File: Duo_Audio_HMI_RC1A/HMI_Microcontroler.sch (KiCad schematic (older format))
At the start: 28 parts, among them P4 HEADER_5X2_P0.05, U1 LPC175XFBD80, U2 TLV803, U3 74LVC1G125, X1 10MHz

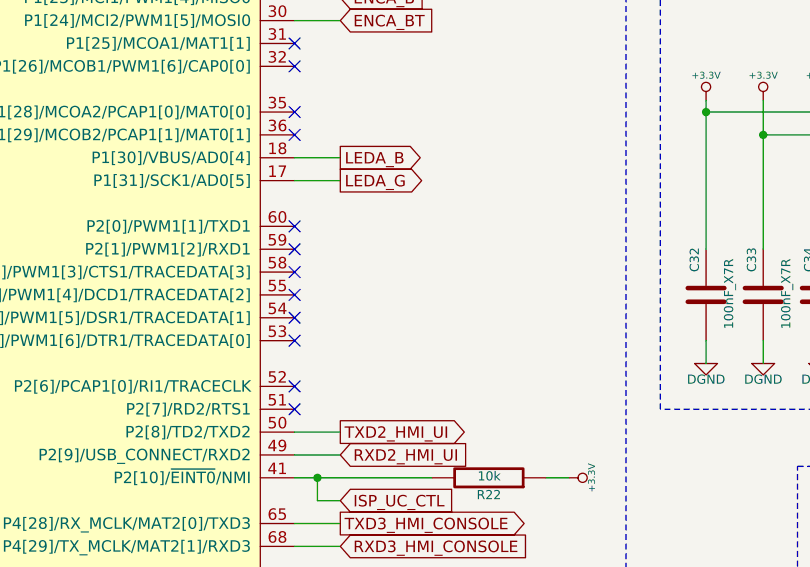
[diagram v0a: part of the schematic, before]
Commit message: Implementing RCA1 schematic  modifications for new layout. Backup commit.
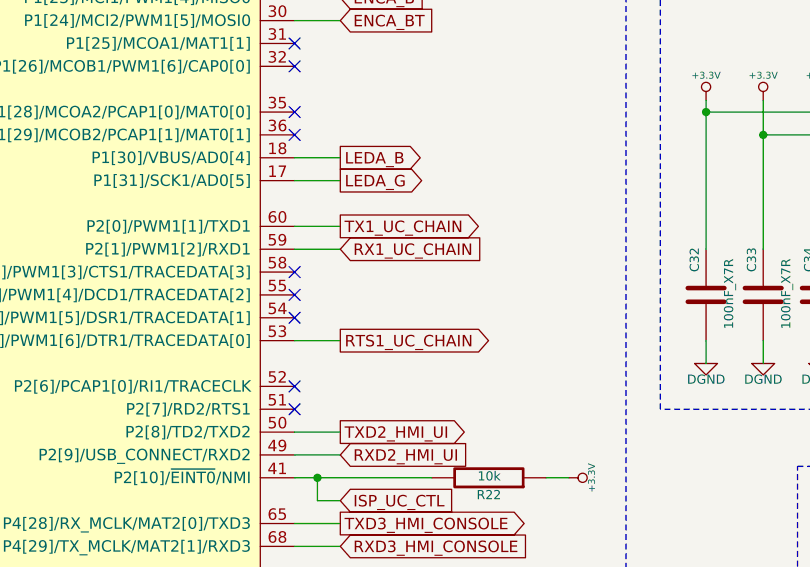
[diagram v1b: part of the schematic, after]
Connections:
- net RTS1_UC_CHAIN: now reaches U1.53 (P2[5]/PWM1[6]/DTR1/TRACEDATA[0])
- net RX1_UC_CHAIN: now reaches U1.59 (P2[1]/PWM1[2]/RXD1)
- net TX1_UC_CHAIN: now reaches U1.60 (P2[0]/PWM1[1]/TXD1)
- no-connect marks 28 -> 25
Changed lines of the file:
@@
 Text GLabel 2200 1750 0    50   Input ~ 0
 RXD0_HMI_FIRMWARE
-NoConn ~ 5600 2850
-NoConn ~ 5600 2950
 NoConn ~ 5600 3050
 NoConn ~ 5600 3150
 NoConn ~ 5600 3250
-NoConn ~ 5600 3350
+NoConn ~ 5600 3650
 NoConn ~ 5600 3550
-NoConn ~ 5600 3650
 NoConn ~ 2400 1450
 NoConn ~ 2400 1550
@@
 	5700 4050 5700 3950
 Connection ~ 5700 3950
+Text GLabel 5800 2850 2    50   Output ~ 0
+TX1_UC_CHAIN
+Text GLabel 5800 2950 2    50   Input ~ 0
+RX1_UC_CHAIN
+Text GLabel 5800 3350 2    50   Output ~ 0
+RTS1_UC_CHAIN
+Wire Wire Line
+	5600 2850 5800 2850
+Wire Wire Line
+	5600 2950 5800 2950
+Wire Wire Line
+	5600 3350 5800 3350
 $EndSCHEMATC

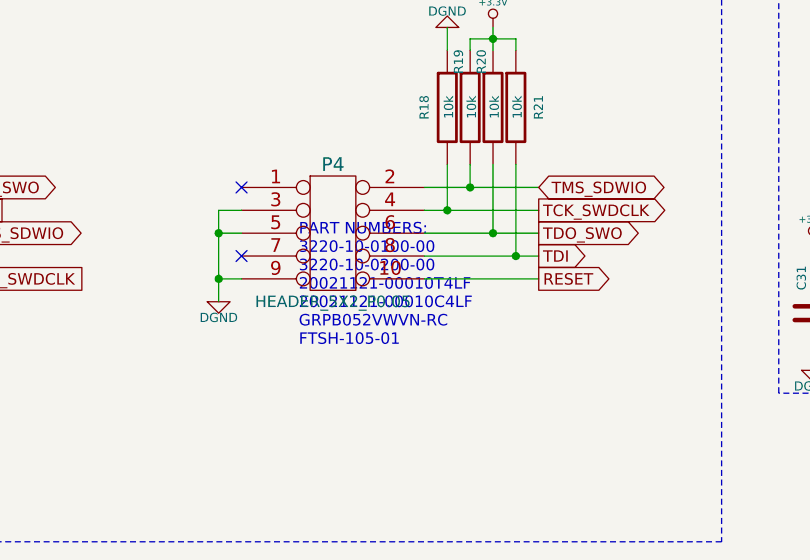
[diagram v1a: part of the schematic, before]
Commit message: Finished RCA1 schematic of the Baseboard and the Pannelboard with USB OTG. Board dimensions, most footprint attribution and major placement implemented in layout. Learning GIT!
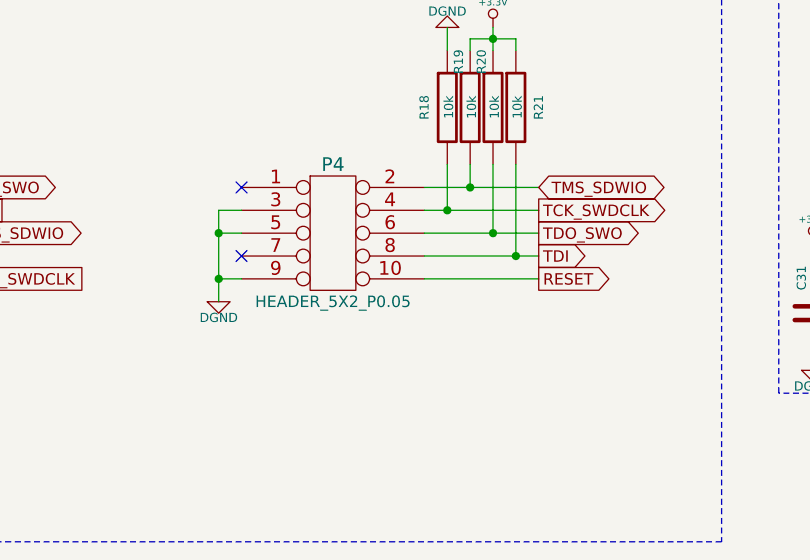
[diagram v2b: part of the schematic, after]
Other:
- note removed: "PART NUMBERS:\n3220-10-0100-00\n3220-10-0200-00\n20021121-00010T4LF\n20021121-00010C4LF\nGRPB052VWVN-RC\nFTSH-105-01"
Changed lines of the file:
@@
 LIBS:Duo_Audio_HMI_RC1A
 LIBS:Duo_Audio_HMI_RC1A-cache
-EELAYER 24 0
+EELAYER 27 0
 EELAYER END
 $Descr A4 11693 8268
@@
 Sheet 4 10
 Title "MOD Duo Baseboard RC1A"
-Date "14 may 2014"
+Date "20 may 2014"
 Rev "RC1A"
 Comp ""
@@
 $EndComp
 $Comp
-L DGND #PWR80
+L DGND #PWR051
 U 1 1 5320BC1F
 P 10650 6100
-F 0 "#PWR80" H 10650 6100 40  0001 C CNN
+F 0 "#PWR051" H 10650 6100 40  0001 C CNN
 F 1 "DGND" H 10650 6030 40  0000 C CNN
 F 2 "~" H 10650 6100 60  0000 C CNN
@@
 $EndComp
 $Comp
-L DGND #PWR81
+L DGND #PWR052
 U 1 1 5320BC2C
 P 10650 6900
-F 0 "#PWR81" H 10650 6900 40  0001 C CNN
+F 0 "#PWR052" H 10650 6900 40  0001 C CNN
 F 1 "DGND" H 10650 6830 40  0000 C CNN
 F 2 "~" H 10650 6900 60  0000 C CNN
@@
 $EndComp
 $Comp
-L DGND #PWR57
+L DGND #PWR053
 U 1 1 53210424
 P 6450 6350
-F 0 "#PWR57" H 6450 6350 40  0001 C CNN
+F 0 "#PWR053" H 6450 6350 40  0001 C CNN
 F 1 "DGND" H 6450 6280 40  0000 C CNN
 F 2 "~" H 6450 6350 60  0000 C CNN
@@
 $EndComp
 $Comp
-L +3.3V #PWR55
+L +3.3V #PWR054
 U 1 1 532104A7
 P 5500 6400
-F 0 "#PWR55" H 5500 6360 30  0001 C CNN
+F 0 "#PWR054" H 5500 6360 30  0001 C CNN
 F 1 "+3.3V" H 5500 6510 30  0000 C CNN
 F 2 "~" H 5500 6400 60  0000 C CNN
@@
 $EndComp
 $Comp
-L DGND #PWR59
+L DGND #PWR055
 U 1 1 5321062F
 P 6600 6750
-F 0 "#PWR59" H 6600 6750 40  0001 C CNN
+F 0 "#PWR055" H 6600 6750 40  0001 C CNN
 F 1 "DGND" H 6600 6680 40  0000 C CNN
 F 2 "~" H 6600 6750 60  0000 C CNN
@@
 $EndComp
 $Comp
-L +3.3V #PWR63
+L +3.3V #PWR056
 U 1 1 5321074D
 P 7500 6400
-F 0 "#PWR63" H 7500 6360 30  0001 C CNN
+F 0 "#PWR056" H 7500 6360 30  0001 C CNN
 F 1 "+3.3V" H 7500 6510 30  0000 C CNN
 F 2 "~" H 7500 6400 60  0000 C CNN
@@
 $EndComp
 $Comp
-L +3.3V #PWR58
+L +3.3V #PWR057
 U 1 1 5321098B
 P 6600 5350
-F 0 "#PWR58" H 6600 5310 30  0001 C CNN
+F 0 "#PWR057" H 6600 5310 30  0001 C CNN
 F 1 "+3.3V" H 6600 5460 30  0000 C CNN
 F 2 "~" H 6600 5350 60  0000 C CNN
@@
 RESET_UC_CTL
 $Comp
-L +3.3V #PWR73
+L +3.3V #PWR058
 U 1 1 532115F0
 P 9350 5550
-F 0 "#PWR73" H 9350 5510 30  0001 C CNN
+F 0 "#PWR058" H 9350 5510 30  0001 C CNN
 F 1 "+3.3V" H 9350 5660 30  0000 C CNN
 F 2 "~" H 9350 5550 60  0000 C CNN
@@
 $EndComp
 $Comp
-L DGND #PWR71
+L DGND #PWR059
 U 1 1 53222EE0
 P 8400 2250
-F 0 "#PWR71" H 8400 2250 40  0001 C CNN
+F 0 "#PWR059" H 8400 2250 40  0001 C CNN
 F 1 "DGND" H 8400 2180 40  0000 C CNN
 F 2 "~" H 8400 2250 60  0000 C CNN
@@
 $EndComp
 $Comp
-L DGND #PWR75
+L DGND #PWR060
 U 1 1 5322343A
 P 9850 2150
-F 0 "#PWR75" H 9850 2150 40  0001 C CNN
+F 0 "#PWR060" H 9850 2150 40  0001 C CNN
 F 1 "DGND" H 9850 2080 40  0000 C CNN
 F 2 "~" H 9850 2150 60  0000 C CNN
@@
 $EndComp
 $Comp
-L +3.3V #PWR76
+L +3.3V #PWR061
 U 1 1 5322370A
 P 10250 700
-F 0 "#PWR76" H 10250 660 30  0001 C CNN
+F 0 "#PWR061" H 10250 660 30  0001 C CNN
 F 1 "+3.3V" H 10250 810 30  0000 C CNN
 F 2 "~" H 10250 700 60  0000 C CNN
@@
 $EndComp
 $Comp
-L +3.3V #PWR51
+L +3.3V #PWR062
 U 1 1 53224164
 P 1150 4100
-F 0 "#PWR51" H 1150 4060 30  0001 C CNN
+F 0 "#PWR062" H 1150 4060 30  0001 C CNN
 F 1 "+3.3V" H 1150 4210 30  0000 C CNN
 F 2 "~" H 1150 4100 60  0000 C CNN
@@
 $EndComp
 $Comp
-L +3.3V #PWR61
+L +3.3V #PWR063
 U 1 1 5323ED9E
 P 7400 2300
-F 0 "#PWR61" H 7400 2260 30  0001 C CNN
+F 0 "#PWR063" H 7400 2260 30  0001 C CNN
 F 1 "+3.3V" H 7400 2410 30  0000 C CNN
 F 2 "~" H 7400 2300 60  0000 C CNN
@@
 $EndComp
 $Comp
-L +3.3V #PWR64
+L +3.3V #PWR064
 U 1 1 5323F067
 P 7650 2300
-F 0 "#PWR64" H 7650 2260 30  0001 C CNN
+F 0 "#PWR064" H 7650 2260 30  0001 C CNN
 F 1 "+3.3V" H 7650 2410 30  0000 C CNN
 F 2 "~" H 7650 2300 60  0000 C CNN
@@
 $EndComp
 $Comp
-L +3.3V #PWR69
+L +3.3V #PWR065
 U 1 1 5323F159
 P 8150 2300
-F 0 "#PWR69" H 8150 2260 30  0001 C CNN
+F 0 "#PWR065" H 8150 2260 30  0001 C CNN
 F 1 "+3.3V" H 8150 2410 30  0000 C CNN
 F 2 "~" H 8150 2300 60  0000 C CNN
@@
 $EndComp
 $Comp
-L +3.3V #PWR66
+L +3.3V #PWR066
 U 1 1 5323F193
 P 7900 2300
-F 0 "#PWR66" H 7900 2260 30  0001 C CNN
+F 0 "#PWR066" H 7900 2260 30  0001 C CNN
 F 1 "+3.3V" H 7900 2410 30  0000 C CNN
 F 2 "~" H 7900 2300 60  0000 C CNN
@@
 $EndComp
 $Comp
-L DGND #PWR62
+L DGND #PWR067
 U 1 1 5323F3A6
 P 7400 3450
-F 0 "#PWR62" H 7400 3450 40  0001 C CNN
+F 0 "#PWR067" H 7400 3450 40  0001 C CNN
 F 1 "DGND" H 7400 3380 40  0000 C CNN
 F 2 "~" H 7400 3450 60  0000 C CNN
@@
 $EndComp
 $Comp
-L DGND #PWR65
+L DGND #PWR068
 U 1 1 5323F3AC
 P 7650 3450
-F 0 "#PWR65" H 7650 3450 40  0001 C CNN
+F 0 "#PWR068" H 7650 3450 40  0001 C CNN
 F 1 "DGND" H 7650 3380 40  0000 C CNN
 F 2 "~" H 7650 3450 60  0000 C CNN
@@
 $EndComp
 $Comp
-L DGND #PWR67
+L DGND #PWR069
 U 1 1 5323F3B2
 P 7900 3450
-F 0 "#PWR67" H 7900 3450 40  0001 C CNN
+F 0 "#PWR069" H 7900 3450 40  0001 C CNN
 F 1 "DGND" H 7900 3380 40  0000 C CNN
 F 2 "~" H 7900 3450 60  0000 C CNN
@@
 $EndComp
 $Comp
-L DGND #PWR70
+L DGND #PWR070
 U 1 1 5323F3B8
 P 8150 3450
-F 0 "#PWR70" H 8150 3450 40  0001 C CNN
+F 0 "#PWR070" H 8150 3450 40  0001 C CNN
 F 1 "DGND" H 8150 3380 40  0000 C CNN
 F 2 "~" H 8150 3450 60  0000 C CNN
@@
 $EndComp
 $Comp
-L DGND #PWR77
+L DGND #PWR071
 U 1 1 5323FA79
 P 10250 2550
-F 0 "#PWR77" H 10250 2550 40  0001 C CNN
+F 0 "#PWR071" H 10250 2550 40  0001 C CNN
 F 1 "DGND" H 10250 2480 40  0000 C CNN
 F 2 "~" H 10250 2550 60  0000 C CNN
@@
 $EndComp
 $Comp
-L DGND #PWR79
+L DGND #PWR072
 U 1 1 5323FA86
 P 10550 2550
-F 0 "#PWR79" H 10550 2550 40  0001 C CNN
+F 0 "#PWR072" H 10550 2550 40  0001 C CNN
 F 1 "DGND" H 10550 2480 40  0000 C CNN
 F 2 "~" H 10550 2550 60  0000 C CNN
@@
 $EndComp
 $Comp
-L DGND #PWR83
+L DGND #PWR073
 U 1 1 5323FA93
 P 10900 2550
-F 0 "#PWR83" H 10900 2550 40  0001 C CNN
+F 0 "#PWR073" H 10900 2550 40  0001 C CNN
 F 1 "DGND" H 10900 2480 40  0000 C CNN
 F 2 "~" H 10900 2550 60  0000 C CNN
@@
 $EndComp
 $Comp
-L +3.3V #PWR78
+L +3.3V #PWR074
 U 1 1 53240265
 P 10550 1400
-F 0 "#PWR78" H 10550 1360 30  0001 C CNN
+F 0 "#PWR074" H 10550 1360 30  0001 C CNN
 F 1 "+3.3V" H 10550 1510 30  0000 C CNN
 F 2 "~" H 10550 1400 60  0000 C CNN
@@
 $EndComp
 $Comp
-L +3.3V #PWR82
+L +3.3V #PWR075
 U 1 1 53240367
 P 10900 1400
-F 0 "#PWR82" H 10900 1360 30  0001 C CNN
+F 0 "#PWR075" H 10900 1360 30  0001 C CNN
 F 1 "+3.3V" H 10900 1510 30  0000 C CNN
 F 2 "~" H 10900 1400 60  0000 C CNN
@@
 $EndComp
 $Comp
-L DGND #PWR56
+L DGND #PWR076
 U 1 1 533BFE39
 P 5500 6950
-F 0 "#PWR56" H 5500 6950 40  0001 C CNN
+F 0 "#PWR076" H 5500 6950 40  0001 C CNN
 F 1 "DGND" H 5500 6880 40  0000 C CNN
 F 2 "~" H 5500 6950 60  0000 C CNN
@@
 NTC_TEMP
 $Comp
-L +3.3V #PWR68
+L +3.3V #PWR077
 U 1 1 533B5390
 P 8000 4250
-F 0 "#PWR68" H 8000 4210 30  0001 C CNN
+F 0 "#PWR077" H 8000 4210 30  0001 C CNN
 F 1 "+3.3V" H 8000 4360 30  0000 C CNN
 F 2 "~" H 8000 4250 60  0000 C CNN
@@
 $EndComp
 $Comp
-L DGND #PWR74
+L DGND #PWR078
 U 1 1 533B6C09
 P 9400 4650
-F 0 "#PWR74" H 9400 4650 40  0001 C CNN
+F 0 "#PWR078" H 9400 4650 40  0001 C CNN
 F 1 "DGND" H 9400 4580 40  0000 C CNN
 F 2 "~" H 9400 4650 60  0000 C CNN
@@
 $EndComp
 $Comp
-L DGND #PWR72
+L DGND #PWR079
 U 1 1 533B7450
 P 9300 4350
-F 0 "#PWR72" H 9300 4350 40  0001 C CNN
+F 0 "#PWR079" H 9300 4350 40  0001 C CNN
 F 1 "DGND" H 9300 4280 40  0000 C CNN
 F 2 "~" H 9300 4350 60  0000 C CNN
@@
 $EndComp
 $Comp
-L +3.3V #PWR60
+L +3.3V #PWR080
 U 1 1 5340DCD6
 P 6800 3950
-F 0 "#PWR60" H 6800 3910 30  0001 C CNN
+F 0 "#PWR080" H 6800 3910 30  0001 C CNN
 F 1 "+3.3V" H 6800 4050 30  0000 C CNN
 F 2 "~" H 6800 3950 60  0000 C CNN
@@
 NoConn ~ 2400 4350
 $Comp
-L PWR_FLAG #FLG1
+L PWR_FLAG #FLG081
 U 1 1 5342B0E5
 P 10400 1300
-F 0 "#FLG1" H 10400 1395 30  0001 C CNN
+F 0 "#FLG081" H 10400 1395 30  0001 C CNN
 F 1 "PWR_FLAG" H 10400 1480 30  0000 C CNN
 F 2 "" H 10400 1300 60  0000 C CNN
@@
 $EndComp
 $Comp
-L DGND #PWR52
+L DGND #PWR082
 U 1 1 537593BF
 P 2900 6650
-F 0 "#PWR52" H 2900 6650 40  0001 C CNN
+F 0 "#PWR082" H 2900 6650 40  0001 C CNN
 F 1 "DGND" H 2900 6580 40  0000 C CNN
 F 2 "~" H 2900 6650 60  0000 C CNN
@@
 Wire Wire Line
 	3800 6450 4300 6450
-Text Notes 3250 6850 0    50   ~ 0
-PART NUMBERS:\n3220-10-0100-00\n3220-10-0200-00\n20021121-00010T4LF\n20021121-00010C4LF\nGRPB052VWVN-RC\nFTSH-105-01
 NoConn ~ 3000 6150
 Text GLabel 1750 6150 2    50   Output ~ 0
@@
 Connection ~ 4200 6450
 $Comp
-L DGND #PWR53
+L DGND #PWR083
 U 1 1 53760FA6
 P 3900 5450
-F 0 "#PWR53" H 3900 5450 40  0001 C CNN
+F 0 "#PWR083" H 3900 5450 40  0001 C CNN
 F 1 "DGND" H 3900 5380 40  0000 C CNN
 F 2 "~" H 3900 5450 60  0000 C CNN
@@
 Connection ~ 4100 5500
 $Comp
-L +3.3V #PWR54
+L +3.3V #PWR084
 U 1 1 5376123B
 P 4100 5450
-F 0 "#PWR54" H 4100 5410 30  0001 C CNN
+F 0 "#PWR084" H 4100 5410 30  0001 C CNN
 F 1 "+3.3V" H 4100 5560 30  0000 C CNN
 F 2 "~" H 4100 5450 60  0000 C CNN

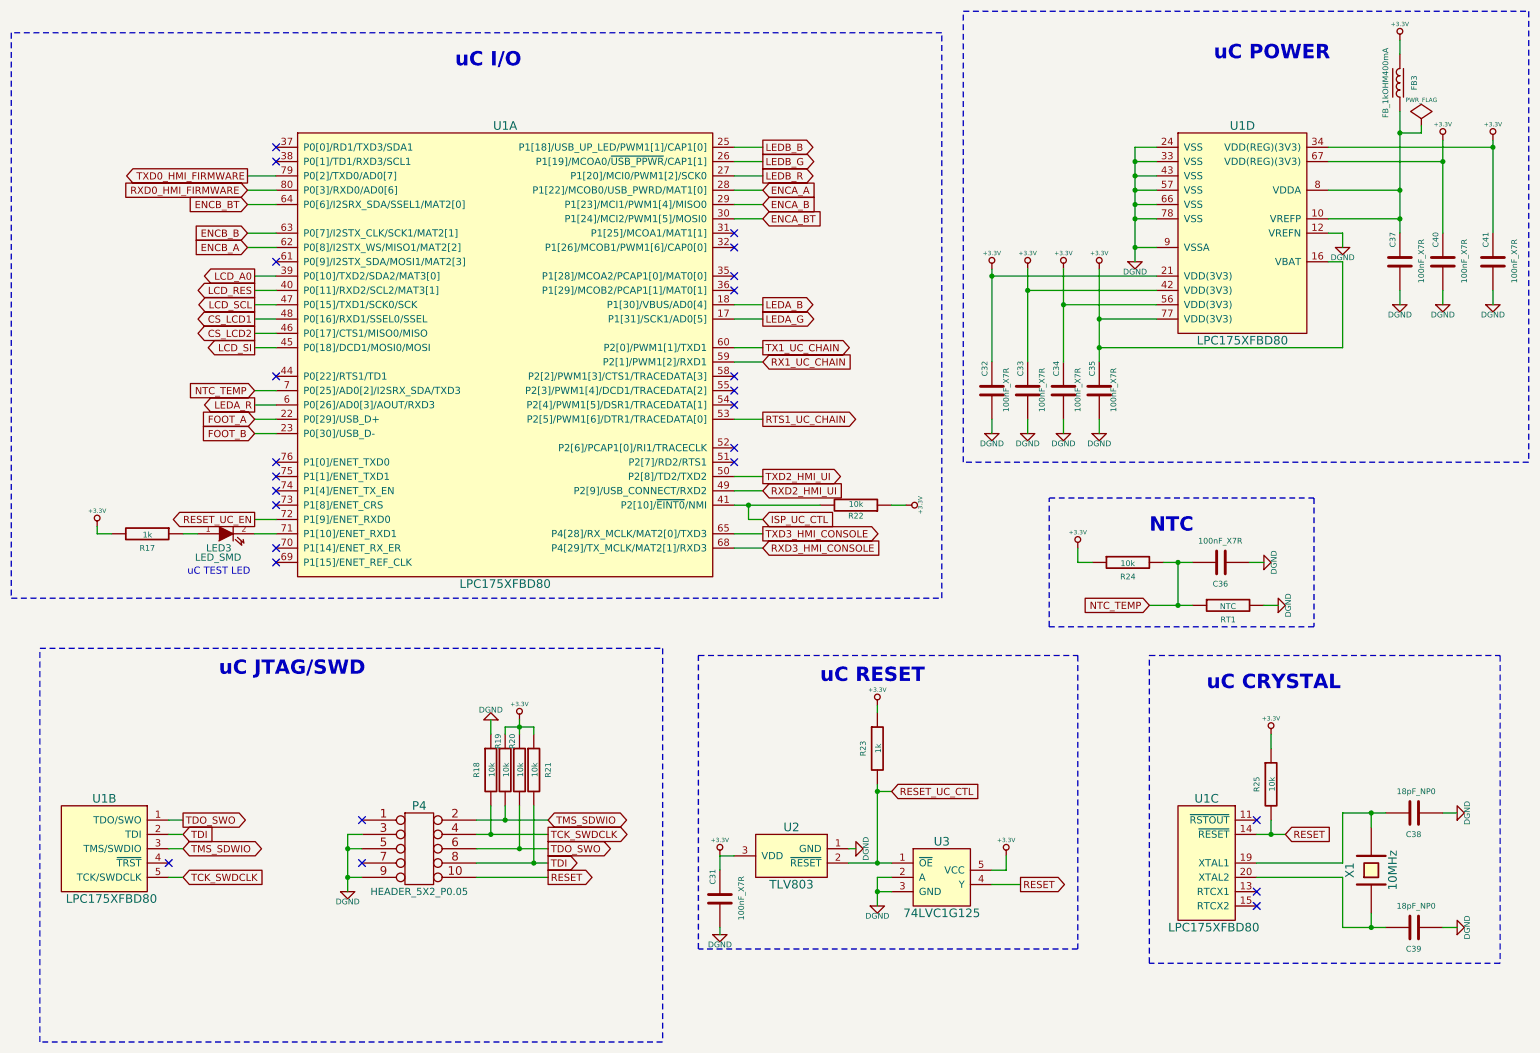
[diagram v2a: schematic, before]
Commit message: Major changes on hardware architecture. Migrating to a HMI separated board. HMI schematic finalized.
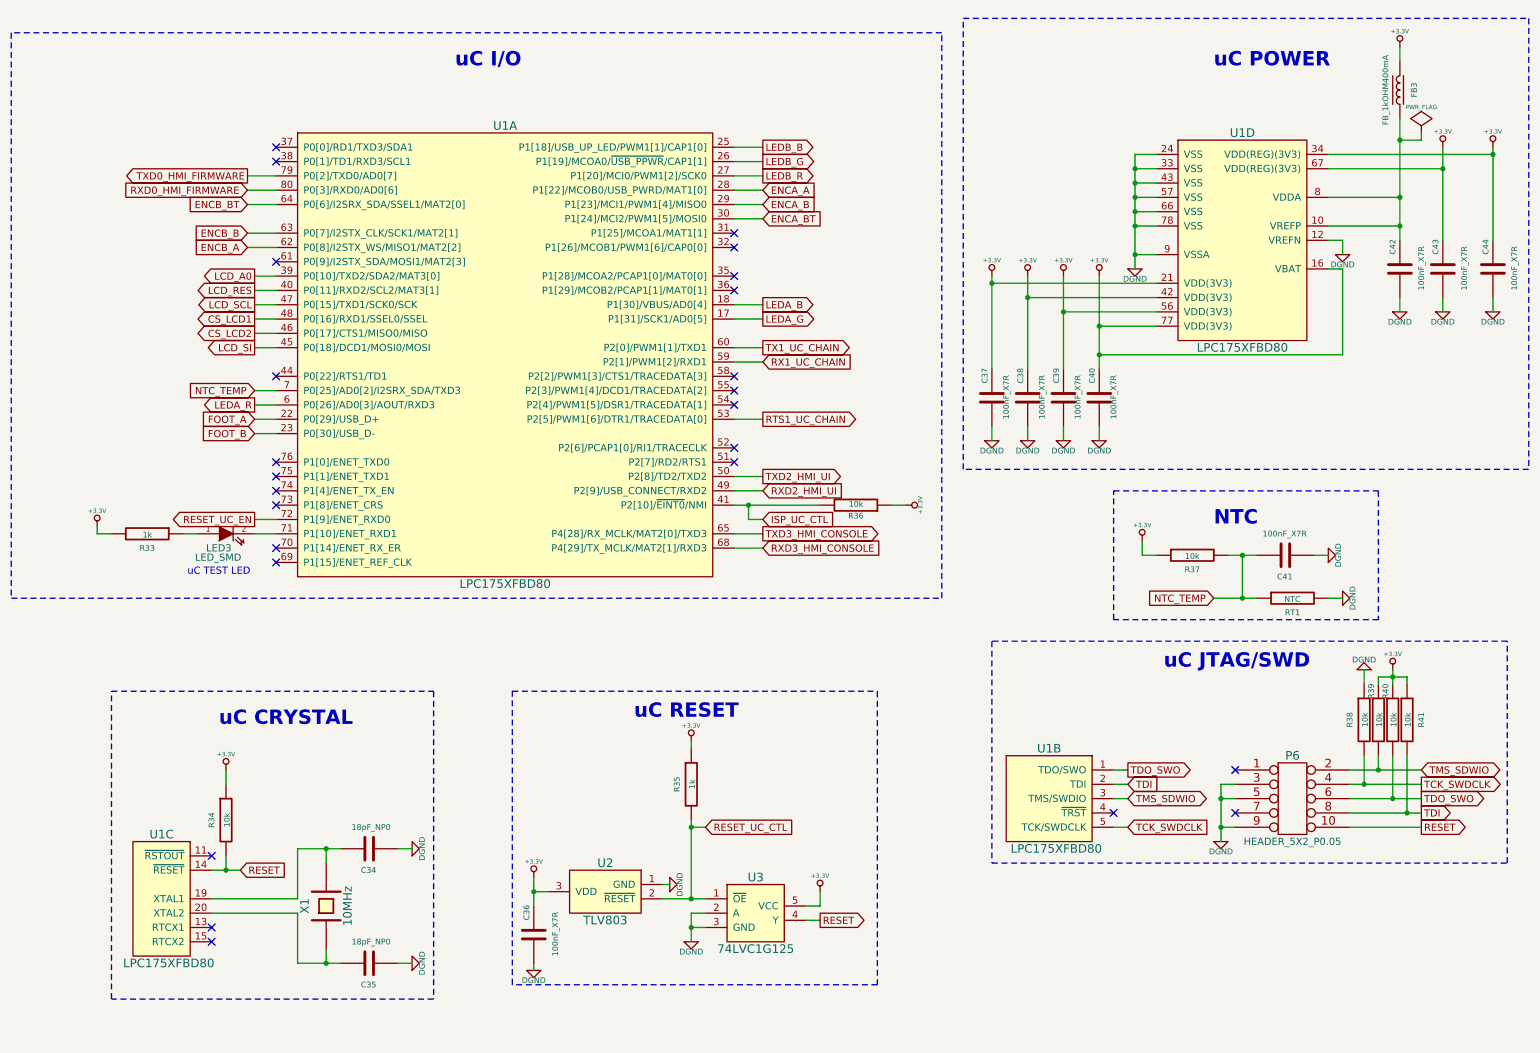
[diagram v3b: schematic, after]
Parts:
- renumbered C38 to C34, C39 to C35, C31 to C36, C32 to C37, C33 to C38, C34 to C39, C35 to C40, C36 to C41, C37 to C42, C40 to C43, C41 to C44, P4 to P6, R17 to R33, R25 to R34, R23 to R35, R22 to R36, R24 to R37, R18 to R38, R19 to R39, R20 to R40, R21 to R41
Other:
- moved on the sheet: C34, C35, C36, C37, C38, C39, C40, C41, C42, C43, C44, FB3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
